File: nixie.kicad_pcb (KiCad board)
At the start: 4 copper layers, 189 x 55 mm, 70 parts, among them J1 Barrel_Jack, J2 Conn_01x02_Pin, Q1 2N3906, Q2 IRF644, SW1 RotaryEncoder_Switch, U1 4504, U2 MC34063AP, U3 HV5222PG-G, U4 LM7805_TO220, U5 HV5222PG-G, U6 ATmega328P-P, U7 DS3231MZ

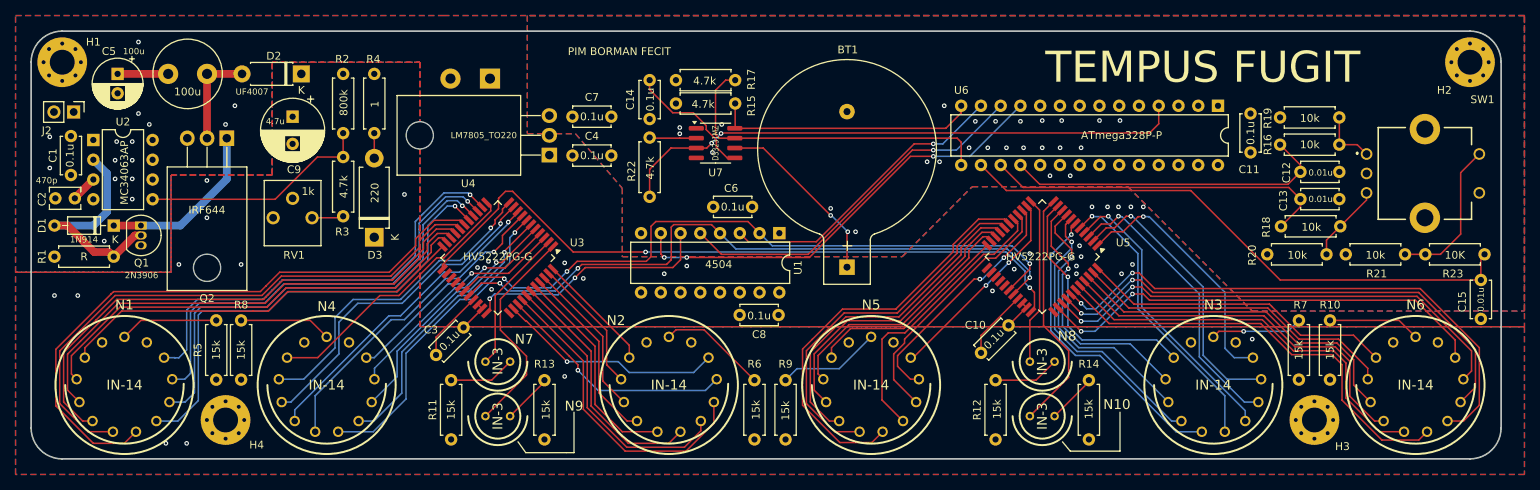
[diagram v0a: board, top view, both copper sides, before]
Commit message: connect scl sda to correct pins
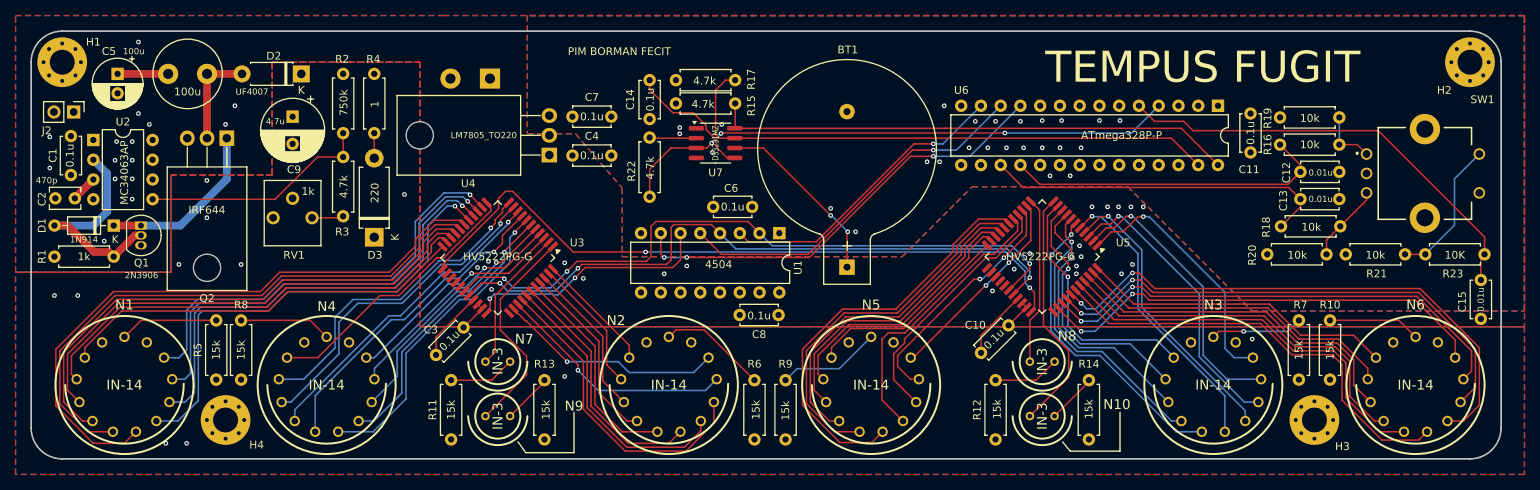
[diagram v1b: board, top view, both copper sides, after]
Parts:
- R1: value R -> 1k
- R2: value 800k -> 750k
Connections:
- U6 pad 14: SCL -> unconnected-(U6-PB0-Pad14)
- U6 pad 15: SDA -> unconnected-(U6-PB1-Pad15)
- U6 pad 16: ROT_PSH -> unconnected-(U6-PB2-Pad16)
- U6 pad 27: unconnected-(U6-PC4-Pad27) -> SDA
- U6 pad 28: unconnected-(U6-PC5-Pad28) -> SCL
- U6 pad 5: unconnected-(U6-PD3-Pad5) -> ROT_PSH
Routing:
- net SCL: track 34.1 -> 67.3 mm
- net SDA: track 43.7 -> 72.4 mm
- net ROT_PSH: track 73.9 -> 57.1 mm
- net SQW: track 73.8 -> 72.4 mm, vias 2 -> 3
- net Net-(R21-Pad2): track 19.5 -> 18.4 mm
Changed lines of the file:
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@@
 	)
 	(property "DATE" "2024-10-13")
-	(property "VERSION" "v1.0")
+	(property "VERSION" "v1.0-1-g7a334a8")
 	(net 0 "")
 	(net 1 "GND")
@@
 	(net 137 "unconnected-(U6-PD0-Pad2)")
 	(net 138 "unconnected-(U6-PB5-Pad19)")
-	(net 139 "unconnected-(U6-PD3-Pad5)")
-	(net 140 "unconnected-(U6-PC4-Pad27)")
+	(net 139 "unconnected-(U6-PB0-Pad14)")
+	(net 140 "unconnected-(U6-PB1-Pad15)")
 	(net 141 "unconnected-(U6-XTAL1{slash}PB6-Pad9)")
-	(net 142 "unconnected-(U6-PC5-Pad28)")
+	(net 142 "unconnected-(U6-PB2-Pad16)")
 	(net 143 "unconnected-(U6-PC0-Pad23)")
 	(net 144 "unconnected-(U7-32KHZ-Pad1)")
@@
 			)
 		)
-		(property "Value" "800k"
+		(property "Value" "750k"
 			(at 3.92 0.08 90)
 			(layer "F.SilkS")
@@
 			(layers "*.Cu" "*.Mask")
 			(remove_unused_layers no)
-			(net 139 "unconnected-(U6-PD3-Pad5)")
+			(net 9 "ROT_PSH")
 			(pinfunction "PD3")
-			(pintype "bidirectional+no_connect")
+			(pintype "bidirectional")
 		)
 		(pad "6" thru_hole oval
@@
 			(layers "*.Cu" "*.Mask")
 			(remove_unused_layers no)
-			(net 102 "SCL")
+			(net 139 "unconnected-(U6-PB0-Pad14)")
 			(pinfunction "PB0")
-			(pintype "bidirectional")
+			(pintype "bidirectional+no_connect")
 		)
 		(pad "15" thru_hole oval
@@
 			(layers "*.Cu" "*.Mask")
 			(remove_unused_layers no)
-			(net 104 "SDA")
+			(net 140 "unconnected-(U6-PB1-Pad15)")
 			(pinfunction "PB1")
-			(pintype "bidirectional")
+			(pintype "bidirectional+no_connect")
 		)
 		(pad "16" thru_hole oval
@@
 			(layers "*.Cu" "*.Mask")
 			(remove_unused_layers no)
-			(net 9 "ROT_PSH")
+			(net 142 "unconnected-(U6-PB2-Pad16)")
 			(pinfunction "PB2")
-			(pintype "bidirectional")
+			(pintype "bidirectional+no_connect")
 		)
 		(pad "17" thru_hole oval
@@
 			(layers "*.Cu" "*.Mask")
 			(remove_unused_layers no)
-			(net 140 "unconnected-(U6-PC4-Pad27)")
+			(net 104 "SDA")
 			(pinfunction "PC4")
-			(pintype "bidirectional+no_connect")
+			(pintype "bidirectional")
 		)
 		(pad "28" thru_hole oval
@@
 			(layers "*.Cu" "*.Mask")
 			(remove_unused_layers no)
-			(net 142 "unconnected-(U6-PC5-Pad28)")
+			(net 102 "SCL")
 			(pinfunction "PC5")
-			(pintype "bidirectional+no_connect")
+			(pintype "bidirectional")
 		)
 		(model "${KIPRJMOD}/packages3D/DIP-28_W7.62mm.wrl"
@@
 			)
 		)
-		(property "Value" "R"
+		(property "Value" "1k"
 			(at 3.81 0 0)
 			(layer "F.SilkS")
@@
 	)
 	(segment
-		(start 258.4 93)
-		(end 258.4 90.1695)
+		(start 216.44 72.6)
+		(end 214.44 70.6)
 		(width 0.2)
 		(layer "F.Cu")
@@
 	)
 	(segment
-		(start 221.1 81.5)
-		(end 197.4 81.5)
+		(start 258.4 93)
+		(end 258.4 90.1695)
 		(width 0.2)
 		(layer "F.Cu")
@@
 	)
 	(segment
-		(start 232.6 93)
-		(end 221.1 81.5)
+		(start 221.4 73.8)
+		(end 220.2 72.6)
 		(width 0.2)
 		(layer "F.Cu")
@@
 	)
 	(segment
-		(start 197.4 81.5)
-		(end 194.12 78.22)
+		(start 258.87 87.47)
+		(end 245.2 73.8)
 		(width 0.2)
 		(layer "F.Cu")
@@
 	)
 	(segment
-		(start 258.4 93)
-		(end 232.6 93)
+		(start 258.87 89.6995)
+		(end 258.87 87.47)
 		(width 0.2)
 		(layer "F.Cu")
@@
 	)
 	(segment
+		(start 245.2 73.8)
+		(end 221.4 73.8)
+		(width 0.2)
+		(layer "F.Cu")
+		(net 9)
+	)
+	(segment
+		(start 220.2 72.6)
+		(end 216.44 72.6)
+		(width 0.2)
+		(layer "F.Cu")
+		(net 9)
+	)
+	(segment
 		(start 85.35 87.27)
 		(end 86.12 87.27)
@@
 	)
 	(segment
-		(start 189.6 73.5)
-		(end 191.58 71.52)
+		(start 189.605 73.495)
+		(end 219.875 73.495)
 		(width 0.2)
 		(layer "F.Cu")
@@
 	)
 	(segment
-		(start 191.58 71.52)
-		(end 191.58 70.6)
+		(start 219.875 73.495)
+		(end 224.6 78.22)
+		(width 0.2)
+		(layer "F.Cu")
+		(net 102)
+	)
+	(segment
+		(start 189.6 73.5)
+		(end 189.605 73.495)
 		(width 0.2)
 		(layer "F.Cu")
@@
 	)
 	(segment
-		(start 240.2 72.1)
+		(start 242.5 75.6)
 		(end 240.2 75.6)
 		(width 0.2)
@@
 	)
 	(segment
-		(start 242.5 75.6)
-		(end 240.2 75.6)
+		(start 243.7 76.8)
+		(end 242.5 75.6)
 		(width 0.2)
 		(layer "F.Cu")
@@
 	)
 	(segment
-		(start 243.7 76.8)
-		(end 242.5 75.6)
+		(start 240.2 72.1)
+		(end 240.2 75.6)
 		(width 0.2)
-		(layer "F.Cu")
+		(layer "B.Cu")
 		(net 103)
 	)
 	(segment
-		(start 162.475 74.765)
-		(end 191.065 74.765)
+		(start 160 74.3)
+		(end 160.465 74.765)
 		(width 0.2)
 		(layer "F.Cu")
@@
 	)
 	(segment
-		(start 160 74.3)
-		(end 160.465 74.765)
+		(start 218.605 74.765)
+		(end 222.06 78.22)
 		(width 0.2)
 		(layer "F.Cu")
@@
 	)
 	(segment
-		(start 160 68.6)
-		(end 160 74.3)
+		(start 162.475 74.765)
+		(end 218.605 74.765)
 		(width 0.2)
 		(layer "F.Cu")
@@
 	)
 	(segment
-		(start 191.065 74.765)
-		(end 191.58 75.28)
+		(start 160 68.6)
+		(end 160 74.3)
 		(width 0.2)
 		(layer "F.Cu")
@@
 	)
 	(segment
-		(start 191.58 75.28)
-		(end 191.58 78.22)
-		(width 0.2)
-		(layer "F.Cu")
-		(net 104)
-	)
-	(segment
 		(start 240.32 86.1)
 		(end 243.7 82.72)
@@
 	)
 	(segment
-		(start 255.8 79.2)
-		(end 255.8 87.1)
-		(width 0.2)
-		(layer "F.Cu")
-		(net 106)
-	)
-	(segment
-		(start 253.2 89.7)
-		(end 253.1995 89.6995)
+		(start 248.65 89.6995)
+		(end 248.7995 89.6995)
 		(width 0.2)
 		(layer "F.Cu")
@@
 	)
 	(segment
-		(start 255.8 87.1)
-		(end 253.2 89.7)
+		(start 248.8 89.7)
+		(end 248.8005 89.6995)
 		(width 0.2)
 		(layer "F.Cu")
@@
 	)
 	(segment
-		(start 248.65 89.6995)
-		(end 248.7995 89.6995)
+		(start 255 85.9495)
+		(end 251.25 89.6995)
 		(width 0.2)
-		(layer "F.Cu")
+		(layer "B.Cu")
 		(net 106)
 	)
 	(segment
 		(start 258.2 76.8)
-		(end 255.8 79.2)
+		(end 255 80)
 		(width 0.2)
-		(layer "F.Cu")
-		(net 106)
-	)
-	(segment
-		(start 253.1995 89.6995)
-		(end 251.25 89.6995)
-		(width 0.2)
-		(layer "F.Cu")
+		(layer "B.Cu")
 		(net 106)
 	)
 	(segment
-		(start 248.8 89.7)
-		(end 248.8005 89.6995)
+		(start 255 80)
+		(end 255 85.9495)
 		(width 0.2)
-		(layer "F.Cu")
+		(layer "B.Cu")
 		(net 106)
 	)
@@
 	)
 	(segment
-		(start 216.98 72.92)
-		(end 216.98 70.6)
-		(width 0.2)
-		(layer "F.Cu")
-		(net 107)
-	)
-	(segment
 		(start 154.335 76.035)
 		(end 157.525 76.035)
@@
 	)
 	(segment
-		(start 160.77 74.095)
-		(end 215.805 74.095)
-		(width 0.2)
-		(layer "F.Cu")
-		(net 107)
-	)
-	(segment
 		(start 151.525 78.775)
 		(end 154.3 76)
@@
 	)
 	(segment
-		(start 215.805 74.095)
-		(end 216.98 72.92)
+		(start 158.865 76.035)
+		(end 157.525 76.035)
 		(width 0.2)
 		(layer "F.Cu")
@@
 	)
 	(segment
-		(start 158.865 76.035)
-		(end 157.525 76.035)
+		(start 151.525 82.305)
+		(end 151.525 78.775)
 		(width 0.2)
 		(layer "F.Cu")
@@
 	)
 	(segment
-		(start 151.525 82.305)
-		(end 151.525 78.775)
+		(start 160.77 74.095)
+		(end 197.2 74.095)
 		(width 0.2)
 		(layer "F.Cu")
@@
 	)
 	(via
+		(at 197.2 74.095)
+		(size 0.6)
+		(drill 0.3)
+		(layers "F.Cu" "B.Cu")
+		(net 107)
+	)
+	(via
 		(at 159.5 75.4)
 		(size 0.6)
@@
 	)
 	(segment
+		(start 197.2 74.095)
+		(end 213.485 74.095)
+		(width 0.2)
+		(layer "B.Cu")
+		(net 107)
+	)
+	(segment
 		(start 159.5 75.4)
 		(end 160.706765 74.193235)
 		(width 0.2)
 		(layer "B.Cu")
+		(net 107)
+	)
+	(segment
+		(start 213.485 74.095)
+		(end 216.98 70.6)
+		(width 0.2)
+		(layer "B.Cu")
